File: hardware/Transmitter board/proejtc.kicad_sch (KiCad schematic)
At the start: 14 parts, among them J1 AudioPlug2, Q1 2N3904, U1 LM358

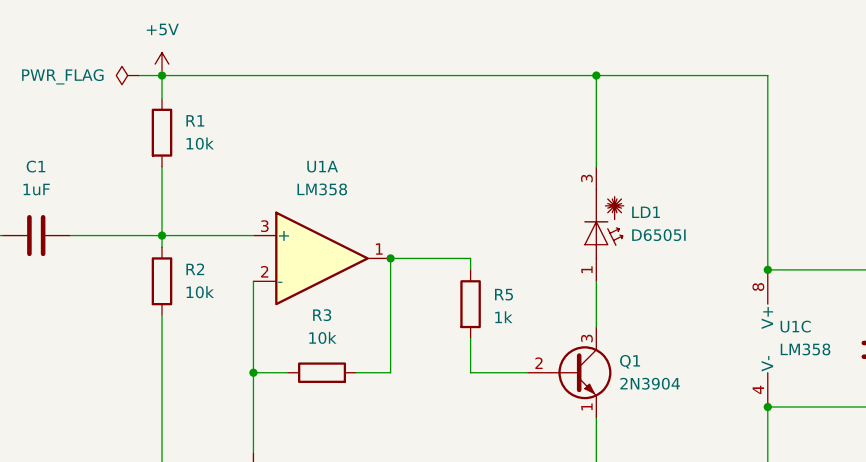
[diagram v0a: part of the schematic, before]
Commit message: fixed biasing of laser diode
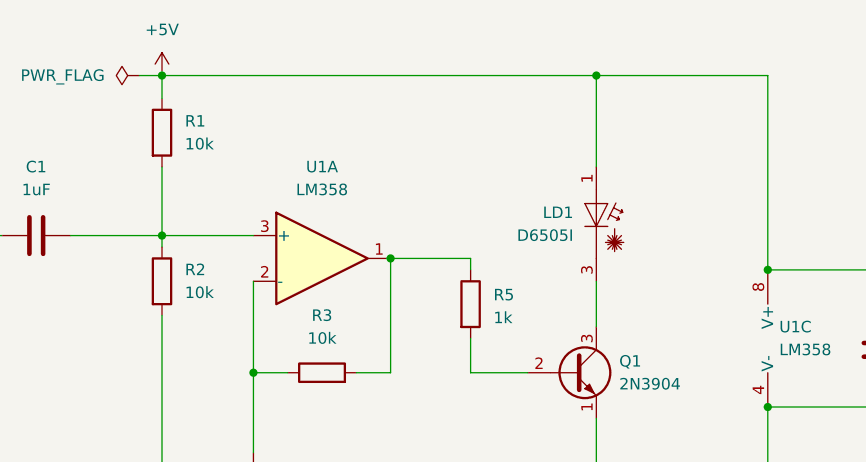
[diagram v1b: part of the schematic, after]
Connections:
- net +5V: now also LD1.1 (A); no longer LD1.3 (C)
- net at Q1.3 (C): now also LD1.3 (C); no longer LD1.1 (A)
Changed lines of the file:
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@@
+	)
+	(junction
+		(at 156.21 52.07)
+		(diameter 0)
+		(color 0 0 0 0)
 	)
 	(junction
@@
 	)
 	(junction
-		(at 156.21 52.07)
-		(diameter 0)
-		(color 0 0 0 0)
-	)
-	(junction
 		(at 118.11 85.09)
 		(diameter 0)
@@
 	(wire
 		(pts
+			(xy 156.21 52.07) (xy 175.26 52.07)
+		)
+		(stroke
+			(width 0)
+			(type default)
+		)
+	)
+	(wire
+		(pts
+			(xy 118.11 101.6) (xy 118.11 105.41)
+		)
+		(stroke
+			(width 0)
+			(type default)
+		)
+	)
+	(wire
+		(pts
+			(xy 156.21 120.65) (xy 175.26 120.65)
+		)
+		(stroke
+			(width 0)
+			(type default)
+		)
+	)
+	(wire
+		(pts
+			(xy 118.11 85.09) (xy 118.11 93.98)
+		)
+		(stroke
+			(width 0)
+			(type default)
+		)
+	)
+	(wire
+		(pts
+			(xy 107.95 62.23) (xy 107.95 69.85)
+		)
+		(stroke
+			(width 0)
+			(type default)
+		)
+	)
+	(wire
+		(pts
+			(xy 118.11 120.65) (xy 156.21 120.65)
+		)
+		(stroke
+			(width 0)
+			(type default)
+		)
+	)
+	(wire
+		(pts
+			(xy 114.3 127) (xy 118.11 127)
+		)
+		(stroke
+			(width 0)
+			(type default)
+		)
+	)
+	(wire
+		(pts
+			(xy 156.21 102.87) (xy 156.21 105.41)
+		)
+		(stroke
+			(width 0)
+			(type default)
+		)
+	)
+	(wire
+		(pts
+			(xy 107.95 78.74) (xy 107.95 120.65)
+		)
+		(stroke
+			(width 0)
+			(type default)
+		)
+	)
+	(wire
+		(pts
+			(xy 118.11 113.03) (xy 118.11 120.65)
+		)
+		(stroke
+			(width 0)
+			(type default)
+		)
+	)
+	(wire
+		(pts
+			(xy 107.95 69.85) (xy 107.95 71.12)
+		)
+		(stroke
+			(width 0)
+			(type default)
+		)
+	)
+	(wire
+		(pts
+			(xy 107.95 52.07) (xy 156.21 52.07)
+		)
+		(stroke
+			(width 0)
+			(type default)
+		)
+	)
+	(wire
+		(pts
+			(xy 107.95 69.85) (xy 118.11 69.85)
+		)
+		(stroke
+			(width 0)
+			(type default)
+		)
+	)
+	(wire
+		(pts
+			(xy 156.21 74.93) (xy 156.21 80.01)
+		)
+		(stroke
+			(width 0)
+			(type default)
+		)
+	)
+	(wire
+		(pts
+			(xy 156.21 113.03) (xy 156.21 120.65)
+		)
+		(stroke
+			(width 0)
+			(type default)
+		)
+	)
+	(wire
+		(pts
+			(xy 105.41 52.07) (xy 107.95 52.07)
+		)
+		(stroke
+			(width 0)
+			(type default)
+		)
+	)
+	(wire
+		(pts
+			(xy 142.24 73.66) (xy 142.24 72.39)
+		)
+		(stroke
+			(width 0)
+			(type default)
+		)
+	)
+	(wire
+		(pts
+			(xy 107.95 120.65) (xy 118.11 120.65)
+		)
+		(stroke
+			(width 0)
+			(type default)
+		)
+	)
+	(wire
+		(pts
+			(xy 133.35 85.09) (xy 133.35 72.39)
+		)
+		(stroke
+			(width 0)
+			(type default)
+		)
+	)
+	(wire
+		(pts
+			(xy 187.96 78.74) (xy 187.96 73.66)
+		)
+		(stroke
+			(width 0)
+			(type default)
+		)
+	)
+	(wire
+		(pts
+			(xy 156.21 90.17) (xy 156.21 95.25)
+		)
+		(stroke
+			(width 0)
+			(type default)
+		)
+	)
+	(wire
+		(pts
 			(xy 156.21 52.07) (xy 156.21 62.23)
-		)
-		(stroke
-			(width 0)
-			(type default)
-		)
-	)
-	(wire
-		(pts
-			(xy 118.11 101.6) (xy 118.11 105.41)
-		)
-		(stroke
-			(width 0)
-			(type default)
-		)
-	)
-	(wire
-		(pts
-			(xy 156.21 120.65) (xy 175.26 120.65)
-		)
-		(stroke
-			(width 0)
-			(type default)
-		)
-	)
-	(wire
-		(pts
-			(xy 118.11 85.09) (xy 118.11 93.98)
-		)
-		(stroke
-			(width 0)
-			(type default)
-		)
-	)
-	(wire
-		(pts
-			(xy 156.21 52.07) (xy 175.26 52.07)
-		)
-		(stroke
-			(width 0)
-			(type default)
-		)
-	)
-	(wire
-		(pts
-			(xy 107.95 62.23) (xy 107.95 69.85)
-		)
-		(stroke
-			(width 0)
-			(type default)
-		)
-	)
-	(wire
-		(pts
-			(xy 118.11 120.65) (xy 156.21 120.65)
-		)
-		(stroke
-			(width 0)
-			(type default)
-		)
-	)
-	(wire
-		(pts
-			(xy 114.3 127) (xy 118.11 127)
-		)
-		(stroke
-			(width 0)
-			(type default)
-		)
-	)
-	(wire
-		(pts
-			(xy 156.21 102.87) (xy 156.21 105.41)
-		)
-		(stroke
-			(width 0)
-			(type default)
-		)
-	)
-	(wire
-		(pts
-			(xy 107.95 78.74) (xy 107.95 120.65)
-		)
-		(stroke
-			(width 0)
-			(type default)
-		)
-	)
-	(wire
-		(pts
-			(xy 118.11 113.03) (xy 118.11 120.65)
-		)
-		(stroke
-			(width 0)
-			(type default)
-		)
-	)
-	(wire
-		(pts
-			(xy 107.95 69.85) (xy 107.95 71.12)
-		)
-		(stroke
-			(width 0)
-			(type default)
-		)
-	)
-	(wire
-		(pts
-			(xy 156.21 52.07) (xy 107.95 52.07)
-		)
-		(stroke
-			(width 0)
-			(type default)
-		)
-	)
-	(wire
-		(pts
-			(xy 107.95 69.85) (xy 118.11 69.85)
-		)
-		(stroke
-			(width 0)
-			(type default)
-		)
-	)
-	(wire
-		(pts
-			(xy 156.21 74.93) (xy 156.21 80.01)
-		)
-		(stroke
-			(width 0)
-			(type default)
-		)
-	)
-	(wire
-		(pts
-			(xy 156.21 113.03) (xy 156.21 120.65)
-		)
-		(stroke
-			(width 0)
-			(type default)
-		)
-	)
-	(wire
-		(pts
-			(xy 105.41 52.07) (xy 107.95 52.07)
-		)
-		(stroke
-			(width 0)
-			(type default)
-		)
-	)
-	(wire
-		(pts
-			(xy 142.24 73.66) (xy 142.24 72.39)
-		)
-		(stroke
-			(width 0)
-			(type default)
-		)
-	)
-	(wire
-		(pts
-			(xy 107.95 120.65) (xy 118.11 120.65)
-		)
-		(stroke
-			(width 0)
-			(type default)
-		)
-	)
-	(wire
-		(pts
-			(xy 133.35 85.09) (xy 133.35 72.39)
-		)
-		(stroke
-			(width 0)
-			(type default)
-		)
-	)
-	(wire
-		(pts
-			(xy 187.96 78.74) (xy 187.96 73.66)
-		)
-		(stroke
-			(width 0)
-			(type default)
-		)
-	)
-	(wire
-		(pts
-			(xy 156.21 90.17) (xy 156.21 95.25)
 		)
 		(stroke
@@
 	(symbol
 		(lib_id "Diode_Laser:PL520")
-		(at 156.21 69.85 270)
+		(at 156.21 67.31 270)
+		(mirror x)
 		(unit 1)
 		(exclude_from_sim no)
@@
 		(on_board yes)
 		(dnp no)
-		(fields_autoplaced yes)
 		(property "Reference" "LD1"
-			(at 160.02 67.3099 90)
-			(effects
-				(font
-					(size 1.27 1.27)
-				)
-				(justify left)
+			(at 153.67 67.3099 90)
+			(effects
+				(font
+					(size 1.27 1.27)
+				)
+				(justify right)
 			)
 		)
 		(property "Value" "D6505I"
-			(at 160.02 69.8499 90)
-			(effects
-				(font
-					(size 1.27 1.27)
-				)
-				(justify left)
+			(at 153.67 69.8499 90)
+			(effects
+				(font
+					(size 1.27 1.27)
+				)
+				(justify right)
 			)
 		)
 		(property "Footprint" "OptoDevice:LaserDiode_TO38ICut-3"
-			(at 151.765 69.85 0)
+			(at 151.765 67.31 0)
 			(effects
 				(font
@@
 		)
 		(property "Datasheet" "http://www.osram-os.com/Graphics/XPic7/00234693_0.pdf/PL%20520.pdf"
-			(at 151.13 70.612 0)
+			(at 151.13 66.548 0)
 			(effects
 				(font
@@
 		)
 		(property "Description" "Green Laser Diode (520nm), TO-38"
-			(at 156.21 69.85 0)
-			(effects
-				(font
+			(at 156.21 67.31 0)
+			(effects
+				(font
